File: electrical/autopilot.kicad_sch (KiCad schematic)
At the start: 6 parts

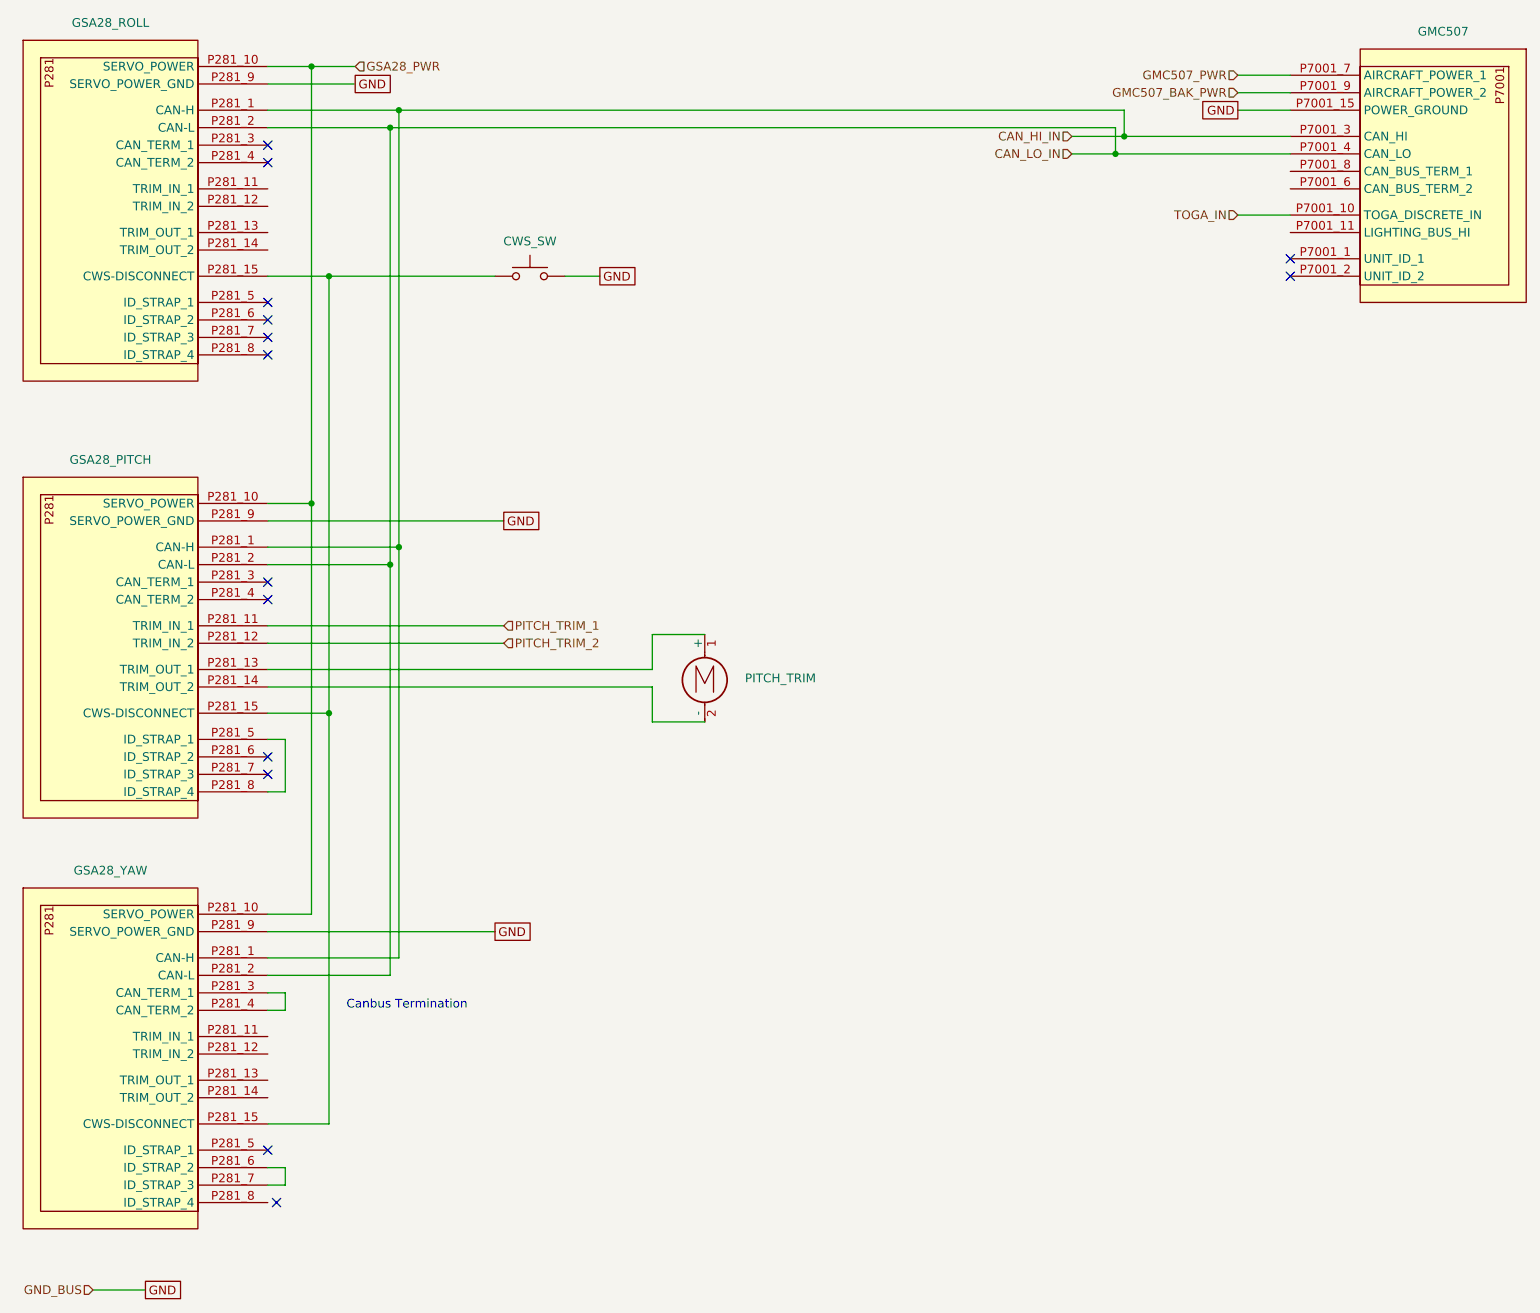
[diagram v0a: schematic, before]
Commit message: Rewired canbus to match physical order.
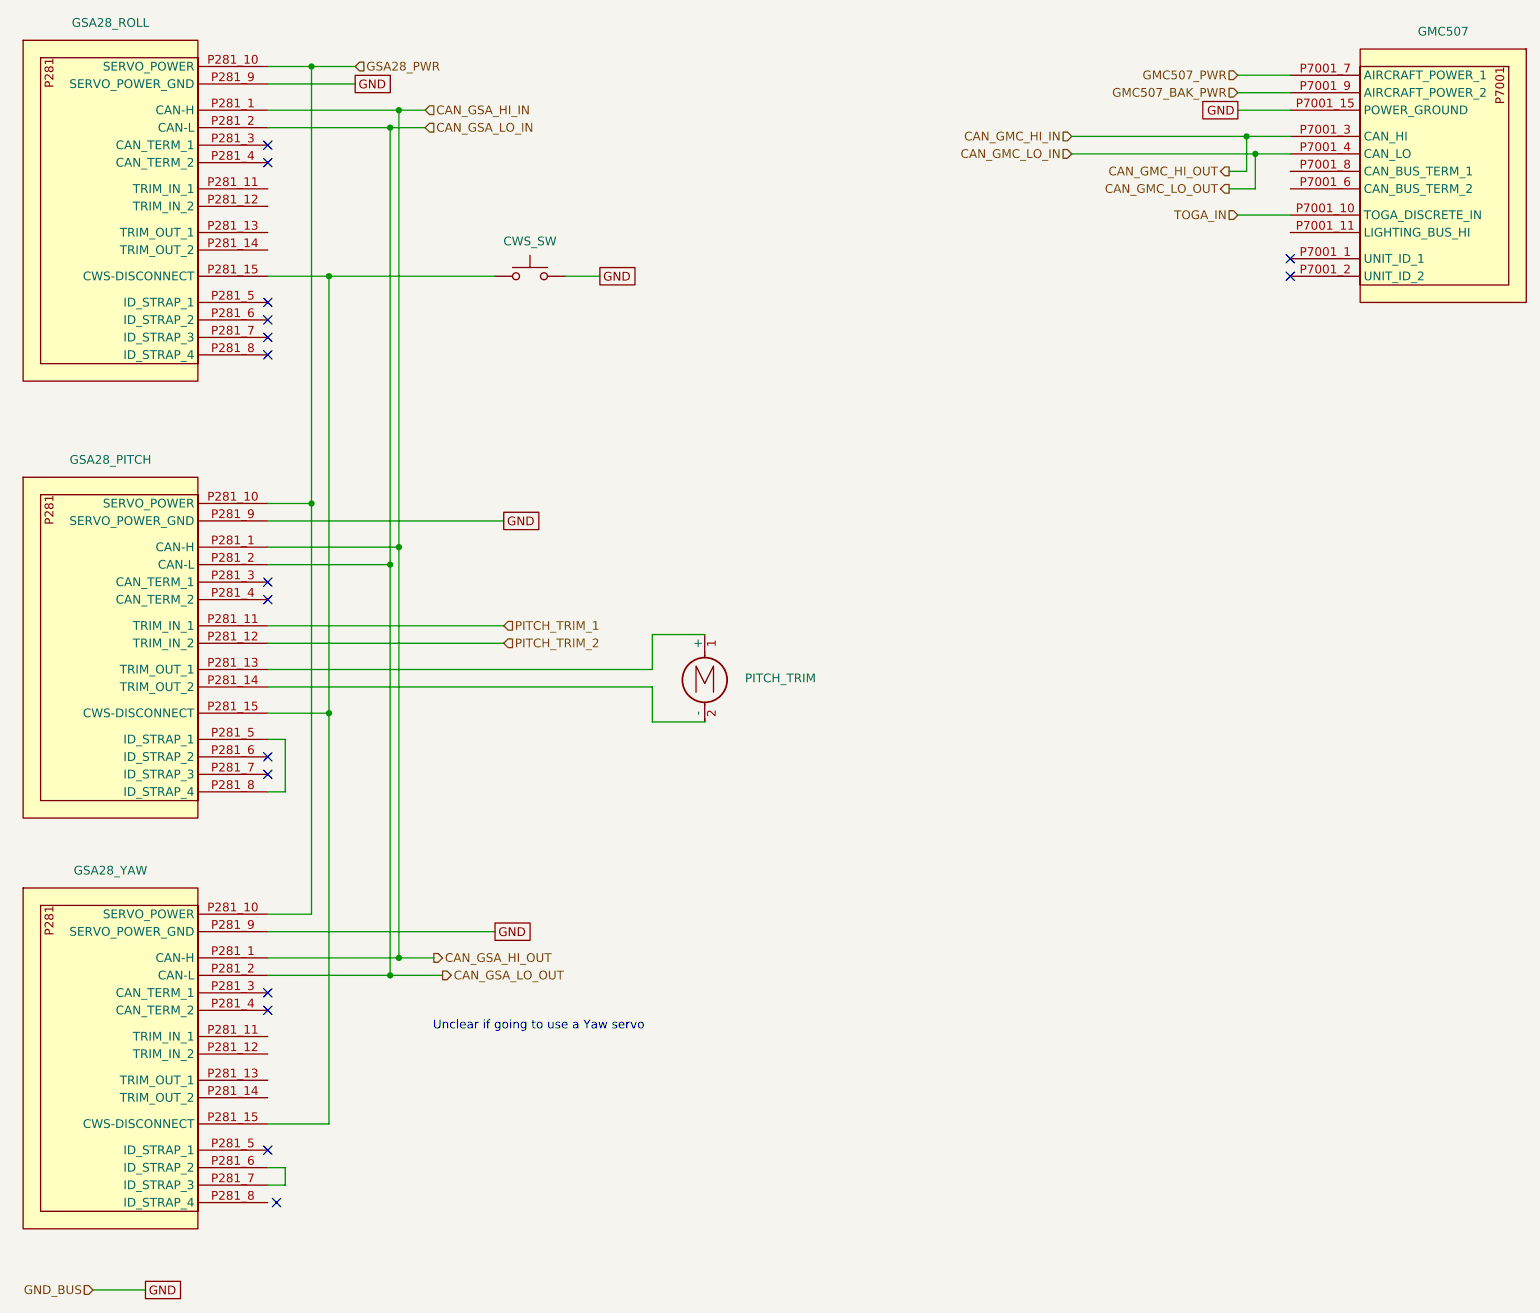
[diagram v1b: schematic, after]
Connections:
- net at GSA28_YAW.P281_3 (CAN_TERM_1): no longer GSA28_YAW.P281_4 (CAN_TERM_2)
- net CAN_HI_IN renamed CAN_GSA_HI_IN
- net CAN_GSA_HI_IN: no longer GMC507.P7001_3 (CAN_HI)
- net CAN_LO_IN renamed CAN_GSA_LO_IN
- net CAN_GSA_LO_IN: no longer GMC507.P7001_4 (CAN_LO)
- new net CAN_GMC_HI_IN: GMC507.P7001_3 (CAN_HI)
- new net CAN_GMC_LO_IN: GMC507.P7001_4 (CAN_LO)
- no-connect marks 14 -> 16
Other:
- note added: "Unclear if going to use a Yaw servo"
- note removed: "Canbus Termination"
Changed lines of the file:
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@@
 	(title_block
 		(title "Autopilot")
-		(date "2025-09-08")
-		(rev "1.0")
+		(date "2025-09-09")
+		(rev "1.0.3")
 		(company "N78HR")
 	)
-	(text "Canbus Termination"
+	(text "Unclear if going to use a Yaw servo"
 		(exclude_from_sim no)
-		(at 67.31 160.02 0)
-		(effects
-			(font
-				(size 1.27 1.27)
-			)
-			(justify left bottom)
+		(at 95.25 162.306 0)
+		(effects
+			(font
+				(size 1.27 1.27)
+			)
 		)
 	)
@@
 	)
 	(junction
-		(at 180.34 33.02)
-		(diameter 0)
-		(color 0 0 0 0)
-	)
-	(junction
 		(at 62.23 22.86)
 		(diameter 0)
@@
 	)
 	(junction
+		(at 199.39 35.56)
+		(diameter 0)
+		(color 0 0 0 0)
+	)
+	(junction
+		(at 74.93 152.4)
+		(diameter 0)
+		(color 0 0 0 0)
+	)
+	(junction
 		(at 74.93 29.21)
 		(diameter 0)
@@
 	)
 	(junction
+		(at 73.66 154.94)
+		(diameter 0)
+		(color 0 0 0 0)
+	)
+	(junction
+		(at 198.12 33.02)
+		(diameter 0)
+		(color 0 0 0 0)
+	)
+	(junction
+		(at 64.77 53.34)
+		(diameter 0)
+		(color 0 0 0 0)
+	)
+	(junction
 		(at 73.66 31.75)
 		(diameter 0)
 		(color 0 0 0 0)
 	)
-	(junction
-		(at 64.77 53.34)
-		(diameter 0)
-		(color 0 0 0 0)
-	)
-	(junction
-		(at 179.07 35.56)
-		(diameter 0)
-		(color 0 0 0 0)
+	(no_connect
+		(at 55.88 157.48)
 	)
 	(no_connect
@@
 	)
 	(no_connect
+		(at 55.88 160.02)
+	)
+	(no_connect
 		(at 55.88 36.83)
 	)
@@
 	(wire
 		(pts
-			(xy 55.88 157.48) (xy 58.42 157.48)
-		)
-		(stroke
-			(width 0)
-			(type default)
-		)
-	)
-	(wire
-		(pts
 			(xy 55.88 95.25) (xy 73.66 95.25)
 		)
@@
 	(wire
 		(pts
-			(xy 180.34 29.21) (xy 180.34 33.02)
-		)
-		(stroke
-			(width 0)
-			(type default)
-		)
-	)
-	(wire
-		(pts
 			(xy 55.88 53.34) (xy 64.77 53.34)
 		)
@@
 	(wire
 		(pts
-			(xy 204.47 35.56) (xy 179.07 35.56)
-		)
-		(stroke
-			(width 0)
-			(type default)
-		)
-	)
-	(wire
-		(pts
 			(xy 55.88 29.21) (xy 74.93 29.21)
 		)
@@
 	(wire
 		(pts
-			(xy 58.42 160.02) (xy 55.88 160.02)
-		)
-		(stroke
-			(width 0)
-			(type default)
-		)
-	)
-	(wire
-		(pts
 			(xy 58.42 182.88) (xy 58.42 185.42)
 		)
@@
 	(wire
 		(pts
-			(xy 58.42 157.48) (xy 58.42 160.02)
-		)
-		(stroke
-			(width 0)
-			(type default)
-		)
-	)
-	(wire
-		(pts
 			(xy 55.88 152.4) (xy 74.93 152.4)
 		)
@@
 	(wire
 		(pts
-			(xy 74.93 29.21) (xy 180.34 29.21)
+			(xy 199.39 35.56) (xy 204.47 35.56)
 		)
 		(stroke
@@
 	(wire
 		(pts
-			(xy 179.07 31.75) (xy 179.07 35.56)
-		)
-		(stroke
-			(width 0)
-			(type default)
-		)
-	)
-	(wire
-		(pts
 			(xy 55.88 176.53) (xy 64.77 176.53)
 		)
@@
 	(wire
 		(pts
+			(xy 195.58 40.64) (xy 199.39 40.64)
+		)
+		(stroke
+			(width 0)
+			(type default)
+		)
+	)
+	(wire
+		(pts
 			(xy 55.88 31.75) (xy 73.66 31.75)
 		)
@@
 	(wire
 		(pts
-			(xy 180.34 33.02) (xy 172.72 33.02)
+			(xy 73.66 31.75) (xy 78.74 31.75)
 		)
 		(stroke
@@
 	(wire
 		(pts
-			(xy 180.34 33.02) (xy 204.47 33.02)
+			(xy 172.72 33.02) (xy 198.12 33.02)
 		)
 		(stroke
@@
 	(wire
 		(pts
+			(xy 198.12 33.02) (xy 204.47 33.02)
+		)
+		(stroke
+			(width 0)
+			(type default)
+		)
+	)
+	(wire
+		(pts
 			(xy 62.23 22.86) (xy 68.58 22.86)
 		)
@@
 	(wire
 		(pts
+			(xy 74.93 152.4) (xy 80.01 152.4)
+		)
+		(stroke
+			(width 0)
+			(type default)
+		)
+	)
+	(wire
+		(pts
+			(xy 73.66 154.94) (xy 81.28 154.94)
+		)
+		(stroke
+			(width 0)
+			(type default)
+		)
+	)
+	(wire
+		(pts
 			(xy 64.77 116.84) (xy 64.77 53.34)
 		)
@@
 	(wire
 		(pts
+			(xy 198.12 38.1) (xy 198.12 33.02)
+		)
+		(stroke
+			(width 0)
+			(type default)
+		)
+	)
+	(wire
+		(pts
 			(xy 196.85 26.67) (xy 204.47 26.67)
 		)
@@
 	(wire
 		(pts
+			(xy 199.39 40.64) (xy 199.39 35.56)
+		)
+		(stroke
+			(width 0)
+			(type default)
+		)
+	)
+	(wire
+		(pts
 			(xy 58.42 128.27) (xy 55.88 128.27)
 		)
@@
 	(wire
 		(pts
-			(xy 179.07 35.56) (xy 172.72 35.56)
+			(xy 172.72 35.56) (xy 199.39 35.56)
 		)
 		(stroke
@@
 	(wire
 		(pts
-			(xy 73.66 31.75) (xy 179.07 31.75)
+			(xy 74.93 29.21) (xy 78.74 29.21)
 		)
 		(stroke
@@
 		(pts
 			(xy 55.88 182.88) (xy 58.42 182.88)
+		)
+		(stroke
+			(width 0)
+			(type default)
+		)
+	)
+	(wire
+		(pts
+			(xy 195.58 38.1) (xy 198.12 38.1)
 		)
 		(stroke
@@
 		)
 	)
-	(hierarchical_label "CAN_HI_IN"
+	(hierarchical_label "CAN_GSA_LO_OUT"
+		(shape output)
+		(at 81.28 154.94 0)
+		(effects
+			(font
+				(size 1.27 1.27)
+			)
+			(justify left)
+		)
+	)
+	(hierarchical_label "CAN_GMC_HI_IN"
 		(shape input)
 		(at 172.72 33.02 180)
@@
 		)
 	)
+	(hierarchical_label "CAN_GSA_HI_IN"
+		(shape input)
+		(at 78.74 29.21 0)
+		(effects
+			(font
+				(size 1.27 1.27)
+			)
+			(justify left)
+		)
+	)
 	(hierarchical_label "GMC507_PWR"
 		(shape input)
@@
 		)
 	)
+	(hierarchical_label "CAN_GMC_LO_OUT"
+		(shape output)
+		(at 195.58 40.64 180)
+		(effects
+			(font
+				(size 1.27 1.27)
+			)
+			(justify right)
+		)
+	)
 	(hierarchical_label "GSA28_PWR"
 		(shape input)
@@
 		)
 	)
-	(hierarchical_label "CAN_LO_IN"
+	(hierarchical_label "CAN_GSA_HI_OUT"
+		(shape output)
+		(at 80.01 152.4 0)
+		(effects
+			(font
+				(size 1.27 1.27)
+			)
+			(justify left)
+		)
+	)
+	(hierarchical_label "CAN_GMC_LO_IN"
 		(shape input)
 		(at 172.72 35.56 180)
@@
 		)
 	)
+	(hierarchical_label "CAN_GMC_HI_OUT"
+		(shape output)
+		(at 195.58 38.1 180)
+		(effects
+			(font
+				(size 1.27 1.27)
+			)
+			(justify right)
+		)
+	)
+	(hierarchical_label "CAN_GSA_LO_IN"
+		(shape input)
+		(at 78.74 31.75 0)
+		(effects
+			(font
+				(size 1.27 1.27)
+			)
+			(justify left)
+		)
+	)

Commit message: Added connectors and non-CAN/RS232/Ethernet shields.
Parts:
- removed CWS_SW: SW_Push, symbol Switch:SW_Push
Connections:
- net CWS: now reaches GSA28_PITCH.P281_15 (CWS-DISCONNECT), GSA28_ROLL.P281_15 (CWS-DISCONNECT), GSA28_YAW.P281_15 (CWS-DISCONNECT)
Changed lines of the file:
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@@
 	(title_block
 		(title "Autopilot")
-		(date "2025-09-09")
-		(rev "1.0.3")
+		(date "2025-10-01")
+		(rev "1.1")
 		(company "N78HR")
 	)
@@
 	)
 	(junction
+		(at 64.77 53.34)
+		(diameter 0)
+		(color 0 0 0 0)
+	)
+	(junction
 		(at 73.66 154.94)
 		(diameter 0)
@@
 	)
 	(junction
-		(at 64.77 53.34)
-		(diameter 0)
-		(color 0 0 0 0)
-	)
-	(junction
 		(at 73.66 31.75)
 		(diameter 0)
@@
 	(wire
 		(pts
+			(xy 64.77 53.34) (xy 78.74 53.34)
+		)
+		(stroke
+			(width 0)
+			(type default)
+		)
+	)
+	(wire
+		(pts
 			(xy 58.42 182.88) (xy 58.42 185.42)
 		)
@@
 	(wire
 		(pts
+			(xy 55.88 88.9) (xy 90.17 88.9)
+		)
+		(stroke
+			(width 0)
+			(type default)
+		)
+	)
+	(wire
+		(pts
 			(xy 111.76 118.11) (xy 111.76 113.03)
 		)
@@
 	(wire
 		(pts
+			(xy 67.31 115.57) (xy 109.22 115.57)
+		)
+		(stroke
+			(width 0)
+			(type dash)
+		)
+	)
+	(wire
+		(pts
 			(xy 55.88 176.53) (xy 64.77 176.53)
 		)
@@
 	(wire
 		(pts
+			(xy 111.76 121.92) (xy 109.22 121.92)
+		)
+		(stroke
+			(width 0)
+			(type default)
+		)
+	)
+	(wire
+		(pts
 			(xy 55.88 104.14) (xy 90.17 104.14)
 		)
@@
 	(wire
 		(pts
-			(xy 99.06 53.34) (xy 104.14 53.34)
-		)
-		(stroke
-			(width 0)
-			(type default)
-		)
-	)
-	(wire
-		(pts
 			(xy 111.76 105.41) (xy 119.38 105.41)
 		)
@@
 	(wire
 		(pts
-			(xy 64.77 53.34) (xy 88.9 53.34)
-		)
-		(stroke
-			(width 0)
-			(type default)
-		)
-	)
-	(wire
-		(pts
 			(xy 30.48 200.66) (xy 38.1 200.66)
 		)
@@
 	(wire
 		(pts
+			(xy 109.22 121.92) (xy 109.22 115.57)
+		)
+		(stroke
+			(width 0)
+			(type default)
+		)
+	)
+	(wire
+		(pts
 			(xy 199.39 40.64) (xy 199.39 35.56)
 		)
@@
 		(pts
 			(xy 111.76 110.49) (xy 111.76 105.41)
-		)
-		(stroke
-			(width 0)
-			(type default)
-		)
-	)
-	(wire
-		(pts
-			(xy 55.88 88.9) (xy 90.17 88.9)
 		)
 		(stroke
@@
 	(global_label "GND"
 		(shape passive)
-		(at 104.14 53.34 0)
-		(fields_autoplaced yes)
-		(effects
-			(font
-				(size 1.27 1.27)
-			)
-			(justify left)
-		)
-		(property "Intersheetrefs" "${INTERSHEET_REFS}"
-			(at 109.8844 53.34 0)
-			(effects
-				(font
-					(size 1.27 1.27)
-				)
-				(justify left)
-				(hide yes)
-			)
-		)
-	)
-	(global_label "GND"
-		(shape passive)
 		(at 90.17 88.9 0)
 		(fields_autoplaced yes)
@@
 	(global_label "GND"
 		(shape passive)
+		(at 111.76 121.92 0)
+		(fields_autoplaced yes)
+		(effects
+			(font
+				(size 1.27 1.27)
+			)
+			(justify left)
+		)
+		(property "Intersheetrefs" "${INTERSHEET_REFS}"
+			(at 117.5044 121.92 0)
+			(effects
+				(font
+					(size 1.27 1.27)
+				)
+				(justify left)
+				(hide yes)
+			)
+		)
+	)
+	(global_label "GND"
+		(shape passive)
 		(at 196.85 29.21 180)
 		(fields_autoplaced yes)
@@
 		)
 	)
+	(hierarchical_label "CWS"
+		(shape input)
+		(at 78.74 53.34 0)
+		(effects
+			(font
+				(size 1.27 1.27)
+			)
+			(justify left)
+		)
+	)
 	(hierarchical_label "GND_BUS"
 		(shape input)
@@
 		)
 	)
-	(symbol
-		(lib_id "Switch:SW_Push")
-		(at 93.98 53.34 0)
-		(unit 1)
-		(exclude_from_sim no)
-		(in_bom yes)
-		(on_board yes)
-		(dnp no)
-		(property "Reference" "CWS_SW"
-			(at 93.98 48.26 0)
-			(effects
-				(font
-					(size 1.27 1.27)
-				)
-			)
-		)
-		(property "Value" "SW_Push"
-			(at 93.98 48.26 0)
-			(effects
-				(font
-					(size 1.27 1.27)
-				)
-				(hide yes)
-			)
-		)
-		(property "Footprint" ""
-			(at 93.98 48.26 0)
-			(effects
-				(font
-					(size 1.27 1.27)
-				)
-				(hide yes)
-			)
-		)
-		(property "Datasheet" "~"
-			(at 93.98 48.26 0)
-			(effects
-				(font
-					(size 1.27 1.27)
-				)
-				(hide yes)
-			)
-		)
-		(property "Description" ""
-			(at 93.98 53.34 0)
-			(effects
-				(font
-					(size 1.27 1.27)
-				)
-			)
-		)
-		(pin "1"
-		)
-		(pin "2"
-		)
-		(instances
-			(project "electrical"
-				(path "/e8ec215a-dbe2-4eba-a577-e50a0a128049/bd38efb0-077c-4462-9d19-e07b49d43233"
-					(reference "CWS_SW")
-					(unit 1)
-				)
-			)
-		)
-	)

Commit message: Added amperage and gauges for wires.
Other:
- note added: "16 AWG"
- note added: "20 AWG"
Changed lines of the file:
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@@
 		(title "Autopilot")
 		(date "2025-10-01")
-		(rev "1.1")
+		(rev "1.1.1")
 		(company "N78HR")
 	)
@@
 		(effects
 			(font
+				(size 1.27 1.27)
+			)
+		)
+	)
+	(text "20 AWG"
+		(exclude_from_sim no)
+		(at 115.062 103.886 0)
+		(effects
+			(font
+				(size 1.27 1.27)
+			)
+		)
+	)
+	(text "16 AWG"
+		(exclude_from_sim no)
+		(at 57.658 83.058 0)
+		(effects
+			(font
+				(size 1.27 1.27)
+			)
+		)
+	)
+	(text "20 AWG"
+		(exclude_from_sim no)
+		(at 83.058 102.616 0)
+		(effects
+			(font
+				(size 1.27 1.27)
+			)
+		)
+	)
+	(text "16 AWG"
+		(exclude_from_sim no)
+		(at 61.976 21.336 0)
+		(effects
+			(font
+				(size 1.27 1.27)
+			)
+		)
+	)
+	(text "16 AWG"
+		(exclude_from_sim no)
+		(at 57.404 143.256 0)
+		(effects
+			(font

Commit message: Added lighting bus
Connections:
- net LIGHTS_HI: now reaches GMC507.P7001_11 (LIGHTING_BUS_HI)
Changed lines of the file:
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@@
 	(title_block
 		(title "Autopilot")
-		(date "2025-10-01")
-		(rev "1.1.1")
+		(date "2025-10-19")
+		(rev "1.1.15")
 		(company "N78HR")
 	)
@@
 		(pts
 			(xy 109.22 121.92) (xy 109.22 115.57)
+		)
+		(stroke
+			(width 0)
+			(type default)
+		)
+	)
+	(wire
+		(pts
+			(xy 196.85 46.99) (xy 204.47 46.99)
 		)
 		(stroke
@@
 		)
 	)
+	(hierarchical_label "LIGHTS_HI"
+		(shape input)
+		(at 196.85 46.99 180)
+		(effects
+			(font
+				(size 1.27 1.27)
+			)
+			(justify right)
+		)
+	)
